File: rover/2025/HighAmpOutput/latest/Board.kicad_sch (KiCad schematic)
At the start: 17 parts, among them J1 JST2_Pin, U1 EC5_Connector, U10 XT60PM-F, U11 XT60PM-F, U12 XT60PM-F, U2 HSS-VN7004SLHTR, U3 XT60-F, U4 XT60-F, U5 XT60-F, U6 XT60-F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

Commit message: .
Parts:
- removed U10, U9: XT60PM-F, RoverFootprint:AMASS_XT60PW-F_1x02_P7.20mm_Horizontal, symbol RoverLibrary:XT60PW-F
- added D2: R, LED_SMD:LED_0805_2012Metric_Pad1.15x1.40mm_HandSolder, symbol RoverLibrary:LED
- added R2: 15k, Resistor_SMD:R_0805_2012Metric_Pad1.20x1.40mm_HandSolder, symbol RoverLibrary:R_0805
- added R5: 1K, Resistor_SMD:R_0805_2012Metric_Pad1.20x1.40mm_HandSolder, symbol RoverLibrary:R_0805
- added U13, U14: XT60-F, RoverFootprint:AMASS_XT60-F_1x02_P7.20mm_Vertical, symbol RoverLibrary:XT60-F
- D1: value LED -> R
- U11, U12: STATUS (none) -> APPROVED
- U2: STATUS TO BE VERIFIED -> APPROVED
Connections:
- net GND: now also R1.2, D2.1 (K), R2.2, U13.1 (-), U14.1 (-); no longer R1.1
- net at J1.1, U2.4 (INPUT): now also R2.1
- net at U2.6 (FR_DIAG): now also R1.1; no longer R1.2
- net +24v renamed +24V
- net +24V: now also R5.1
- net Vinput renamed +24V_I
- net +24V_I: now also U13.2 (+), U14.2 (+)
- new net: D2.2 (A), R5.2
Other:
- moved on the sheet: J1, R1, R4

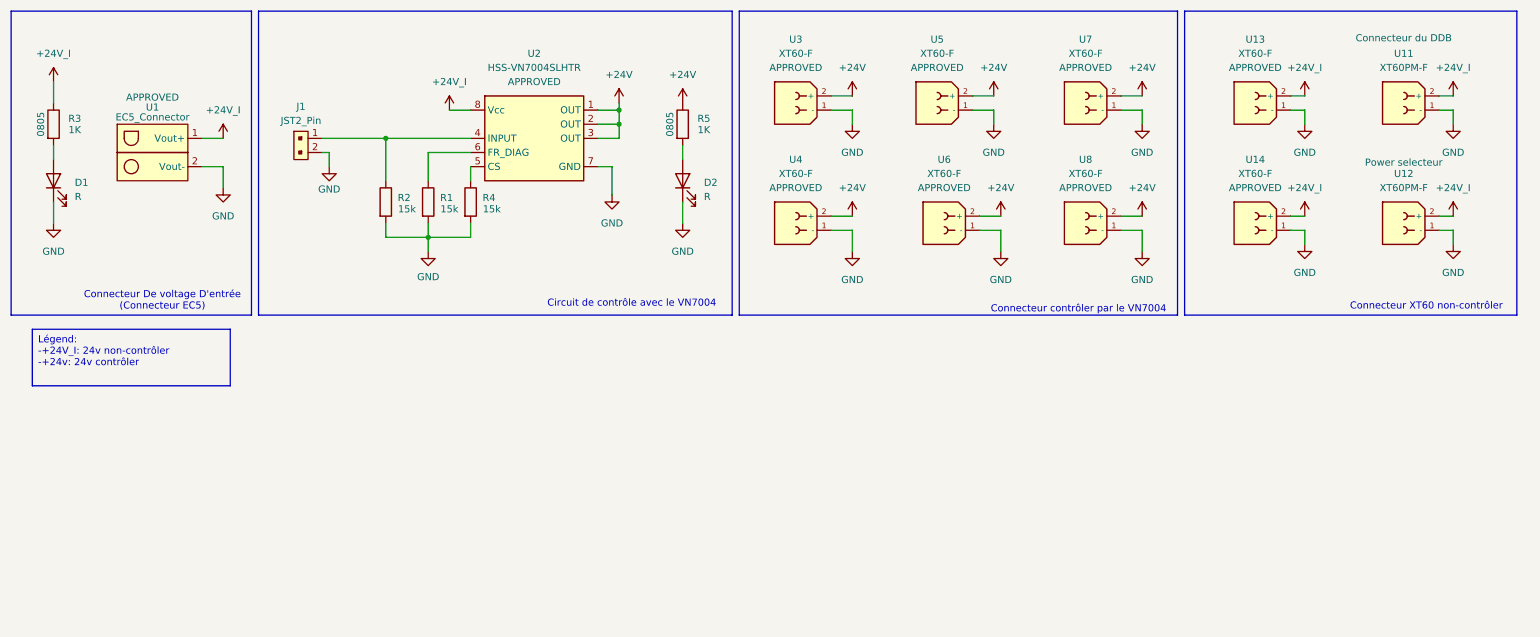
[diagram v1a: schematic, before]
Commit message: Avancement PCB HighAmpOutput
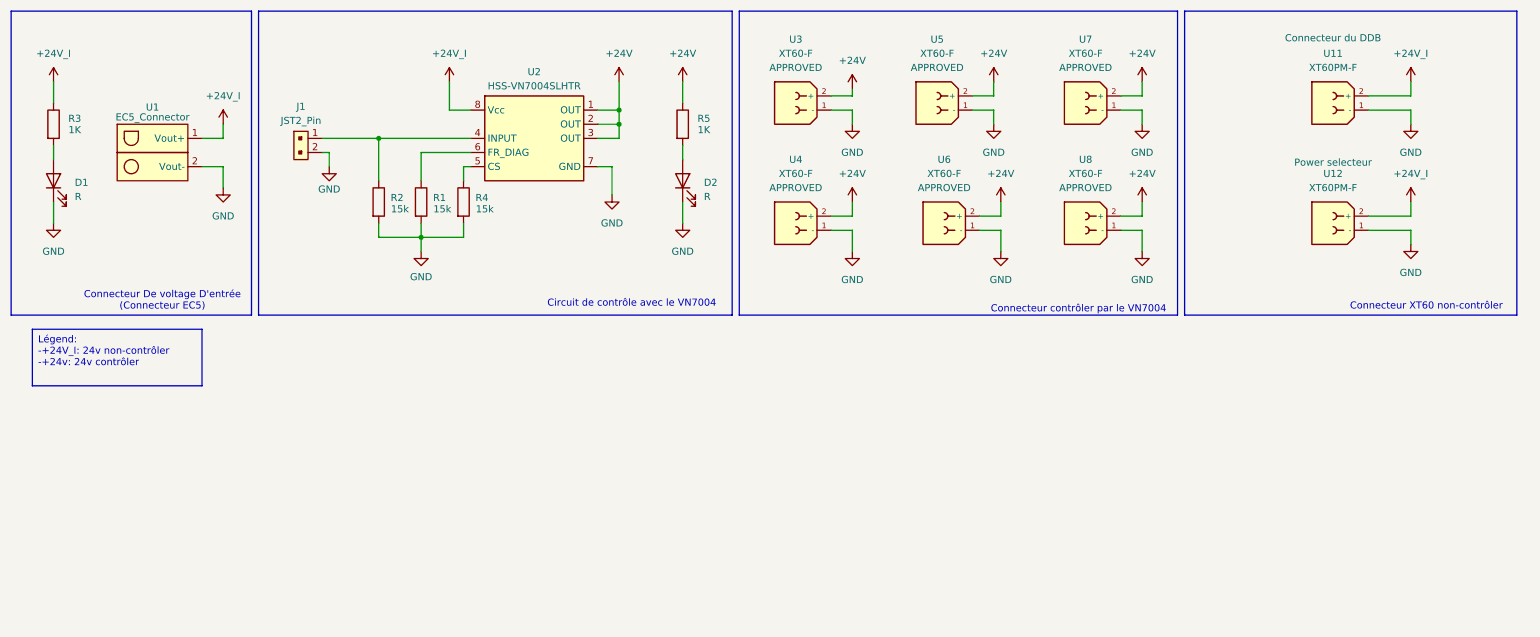
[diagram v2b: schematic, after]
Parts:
- removed U13, U14: XT60-F, RoverFootprint:AMASS_XT60-F_1x02_P7.20mm_Vertical, symbol RoverLibrary:XT60-F
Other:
- moved on the sheet: R1, R2, R4, U11, U12

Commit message: Done
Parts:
- removed J1: JST2_Pin, RoverFootprint:2-pins-JST_XH_B2B-XH-A_1x02_P2.50mm_Vertical, symbol RoverLibrary:CONN-JST-XH-B2B
- added J2: JST-PH-S2B, Connector_JST:JST_PH_B2B-PH-K_1x02_P2.00mm_Vertical, symbol Connector_Generic:Conn_01x02
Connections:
- net GND: now also J2.2 (Pin_2)
- net at R2.1, U2.4 (INPUT): now also J2.1 (Pin_1)
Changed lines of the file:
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@@
 	(wire
 		(pts
-			(xy 69.85 35.56) (xy 80.01 35.56)
+			(xy 72.39 35.56) (xy 80.01 35.56)
 		)
 		(stroke
@@
 	(wire
 		(pts
-			(xy 71.12 38.1) (xy 69.85 38.1)
+			(xy 73.66 38.1) (xy 72.39 38.1)
 		)
 		(stroke
@@
 	(wire
 		(pts
-			(xy 71.12 40.64) (xy 71.12 38.1)
+			(xy 73.66 40.64) (xy 73.66 38.1)
 		)
 		(stroke
@@
 	(symbol
 		(lib_id "power:GND")
-		(at 71.12 40.64 0)
+		(at 73.66 40.64 0)
 		(unit 1)
 		(exclude_from_sim no)
@@
 		(dnp no)
 		(property "Reference" "#PWR06"
-			(at 71.12 46.99 0)
+			(at 73.66 46.99 0)
 			(effects
 				(font
@@
 		)
 		(property "Value" "GND"
-			(at 71.12 44.704 0)
+			(at 73.66 44.704 0)
 			(effects
 				(font
@@
 		)
 		(property "Footprint" ""
-			(at 71.12 40.64 0)
+			(at 73.66 40.64 0)
 			(effects
 				(font
@@
 		)
 		(property "Datasheet" ""
-			(at 71.12 40.64 0)
+			(at 73.66 40.64 0)
 			(effects
 				(font
@@
 		)
 		(property "Description" "Power symbol creates a global label with name \"GND\" , ground"
-			(at 71.12 40.64 0)
+			(at 73.66 40.64 0)
 			(effects
 				(font
@@
 	)
 	(symbol
-		(lib_id "RoverLibrary:CONN-JST-XH-B2B")
-		(at 66.675 32.385 0)
-		(unit 1)
-		(exclude_from_sim no)
-		(in_bom yes)
-		(on_board yes)
-		(dnp no)
-		(fields_autoplaced yes)
-		(property "Reference" "J1"
-			(at 66.04 29.845 0)
-			(effects
-				(font
-					(size 1.27 1.27)
-				)
-			)
-		)
-		(property "Value" "JST2_Pin"
-			(at 66.04 32.385 0)
-			(effects
-				(font
-					(size 1.27 1.27)
-				)
-			)
-		)
-		(property "Footprint" "RoverFootprint:2-pins-JST_XH_B2B-XH-A_1x02_P2.50mm_Vertical"
-			(at 66.675 32.385 0)
-			(effects
-				(font
-					(size 1.27 1.27)
-				)
-				(hide yes)
-			)
-		)
-		(property "Datasheet" ""
-			(at 66.675 32.385 0)
-			(effects
-				(font
-					(size 1.27 1.27)
-				)
-				(hide yes)
-			)
-		)
-		(property "Description" ""
-			(at 66.675 32.385 0)
-			(effects
-				(font
-					(size 1.27 1.27)
-				)
-				(hide yes)
-			)
-		)
-		(pin "1"
-		)
-		(pin "2"
-		)
-		(instances
-			(project "Template"
-				(path "/a4fa9b30-7b48-474a-bdaa-0d7a6d26a697/8da6c8a9-d96a-428b-ac41-906630b726a3"
-					(reference "J1")
-					(unit 1)
-				)
-			)
-		)
-	)
-	(symbol
 		(lib_id "power:GND")
 		(at 134.62 50.8 0)
@@
 					(unit 1)
 				)
+			)
+		)
+	)
+	(symbol
+		(lib_id "Connector_Generic:Conn_01x02")
+		(at 67.31 35.56 0)
+		(mirror y)
+		(unit 1)
+		(exclude_from_sim no)
+		(in_bom yes)
+		(on_board yes)
+		(dnp no)
+		(fields_autoplaced yes)
+		(property "Reference" "J2"
+			(at 67.31 29.21 0)
+			(effects
+				(font
+					(size 1.27 1.27)
+				)
+			)
+		)
+		(property "Value" "JST-PH-S2B"
+			(at 67.31 31.75 0)
+			(effects
+				(font
+					(size 1.27 1.27)
+				)
+			)
+		)
+		(property "Footprint" "Connector_JST:JST_PH_B2B-PH-K_1x02_P2.00mm_Vertical"
+			(at 67.31 35.56 0)
+			(effects
+				(font
+					(size 1.27 1.27)
+				)
+				(hide yes)
+			)
+		)
+		(property "Datasheet" "~"
+			(at 67.31 35.56 0)
+			(effects
+				(font
+					(size 1.27 1.27)
+				)
+				(hide yes)
+			)
+		)
+		(property "Description" "Generic connector, single row, 01x02, script generated (kicad-library-utils/schlib/autogen/connector/)"
+			(at 67.31 35.56 0)
+			(effects
+				(font
+					(size 1.27 1.27)
+				)
+				(hide yes)
+			)
+		)
+		(pin "2"
+		)
+		(pin "1"
+		)
+		(instances
+			(project ""
+				(path "/a4fa9b30-7b48-474a-bdaa-0d7a6d26a697/8da6c8a9-d96a-428b-ac41-906630b726a3"
+					(reference "J2")
+					(unit 1)
+				)

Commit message: HighAmp generated
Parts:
- J2: value JST-PH-S2B -> JST-PH-B2B
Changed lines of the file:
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@@
 			)
 		)
-		(property "Value" "JST-PH-S2B"
+		(property "Value" "JST-PH-B2B"
 			(at 67.31 31.75 0)
 			(effects

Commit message: HighAMP_Rch_ADD_to_INPUT_to_7004
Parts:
- added R6: 15k, Resistor_SMD:R_0805_2012Metric_Pad1.20x1.40mm_HandSolder, symbol RoverLibrary:R_0805
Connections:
- net at J2.1 (Pin_1), R2.1: now also R6.1; no longer U2.4 (INPUT)
- new net: R6.2, U2.4 (INPUT)
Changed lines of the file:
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@@
+	)
+	(junction
+		(at 123.19 30.48)
+		(diameter 0)
+		(color 0 0 0 0)
 	)
 	(junction
@@
 	)
 	(junction
-		(at 123.19 30.48)
-		(diameter 0)
-		(color 0 0 0 0)
-	)
-	(junction
 		(at 123.19 33.02)
 		(diameter 0)
@@
 	(wire
 		(pts
+			(xy 91.44 35.56) (xy 96.52 35.56)
+		)
+		(stroke
+			(width 0)
+			(type default)
+		)
+	)
+	(wire
+		(pts
 			(xy 217.17 52.07) (xy 217.17 55.88)
 		)
@@
 	(wire
 		(pts
+			(xy 80.01 35.56) (xy 83.82 35.56)
+		)
+		(stroke
+			(width 0)
+			(type default)
+		)
+	)
+	(wire
+		(pts
 			(xy 265.43 33.02) (xy 265.43 30.48)
 		)
@@
 		(pts
 			(xy 21.59 25.4) (xy 21.59 29.21)
-		)
-		(stroke
-			(width 0)
-			(type default)
-		)
-	)
-	(wire
-		(pts
-			(xy 80.01 35.56) (xy 96.52 35.56)
 		)
 		(stroke
@@
 					(unit 1)
 				)
+			)
+		)
+	)
+	(symbol
+		(lib_id "RoverLibrary:R_0805")
+		(at 87.63 35.56 90)
+		(unit 1)
+		(exclude_from_sim no)
+		(in_bom yes)
+		(on_board yes)
+		(dnp no)
+		(property "Reference" "R6"
+			(at 88.138 32.512 90)
+			(do_not_autoplace yes)
+			(effects
+				(font
+					(size 1.27 1.27)
+				)
+			)
+		)
+		(property "Value" "15k"
+			(at 87.63 30.48 90)
+			(do_not_autoplace yes)
+			(effects
+				(font
+					(size 1.27 1.27)
+				)
+			)
+		)
+		(property "Footprint" "Resistor_SMD:R_0805_2012Metric_Pad1.20x1.40mm_HandSolder"
+			(at 87.63 43.18 90)
+			(effects
+				(font
+					(size 1.27 1.27)
+				)
+				(hide yes)
+			)
+		)
+		(property "Datasheet" ""
+			(at 87.63 35.56 90)
+			(do_not_autoplace yes)
+			(effects
+				(font
+					(size 1.27 1.27)
+				)
+				(hide yes)
+			)
+		)
+		(property "Description" "Resistor"
+			(at 99.06 35.56 0)
+			(effects
+				(font
+					(size 1.27 1.27)
+				)
+				(hide yes)
+			)
+		)
+		(property "Digikey" ""
+			(at 87.63 35.56 0)
+			(do_not_autoplace yes)
+			(effects
+				(font
+					(size 1.27 1.27)
+				)
+				(hide yes)
+			)
+		)
+		(property "Package" "0805"
+			(at 87.63 37.846 90)
+			(do_not_autoplace yes)
+			(effects
+				(font
+					(size 1.27 1.27)
+				)
+				(hide yes)
+			)
+		)
+		(pin "2"
+		)
+		(pin "1"
+		)
+		(instances
+			(project "HighAmpOutput"
+				(path "/a4fa9b30-7b48-474a-bdaa-0d7a6d26a697/8da6c8a9-d96a-428b-ac41-906630b726a3"
+					(reference "R6")
+					(unit 1)
+				)

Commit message: Update
update pour préparer pour la V2
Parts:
- removed R2: 15k, Resistor_SMD:R_0805_2012Metric_Pad1.20x1.40mm_HandSolder, symbol RoverLibrary:R_0805
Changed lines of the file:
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@@
-	)
-	(junction
-		(at 80.01 35.56)
-		(diameter 0)
-		(color 0 0 0 0)
 	)
 	(junction
@@
 	(wire
 		(pts
-			(xy 72.39 35.56) (xy 80.01 35.56)
-		)
-		(stroke
-			(width 0)
-			(type default)
-		)
-	)
-	(wire
-		(pts
 			(xy 92.71 30.48) (xy 96.52 30.48)
 		)
@@
 	(wire
 		(pts
-			(xy 80.01 35.56) (xy 80.01 43.18)
-		)
-		(stroke
-			(width 0)
-			(type default)
-		)
-	)
-	(wire
-		(pts
 			(xy 52.07 35.56) (xy 52.07 33.02)
 		)
@@
 	(wire
 		(pts
-			(xy 80.01 35.56) (xy 83.82 35.56)
+			(xy 72.39 35.56) (xy 83.82 35.56)
 		)
 		(stroke
@@
 	(wire
 		(pts
-			(xy 80.01 50.8) (xy 80.01 53.34)
-		)
-		(stroke
-			(width 0)
-			(type default)
-		)
-	)
-	(wire
-		(pts
 			(xy 217.17 49.53) (xy 217.17 46.99)
 		)
@@
 		(pts
 			(xy 187.96 49.53) (xy 191.77 49.53)
-		)
-		(stroke
-			(width 0)
-			(type default)
-		)
-	)
-	(wire
-		(pts
-			(xy 80.01 53.34) (xy 87.63 53.34)
 		)
 		(stroke
@@
 				(size 1.27 1.27)
 				(thickness 0.1588)
-				(color 132 0 0 1)
+				(color 0 0 0 1)
+			)
+			(justify left top)
+		)
+	)
+	(text_box "-Ajouter un ventilateur?\n-Dissipation de chaleur répartis sur les différentes layeur"
+		(exclude_from_sim no)
+		(at 139.7 109.22 0)
+		(size 34.29 13.97)
+		(stroke
+			(width 0)
+			(type default)
+			(color 132 0 0 1)
+		)
+		(fill
+			(type color)
+			(color 255 255 194 1)
+		)
+		(effects
+			(font
+				(size 1.27 1.27)
+				(color 0 0 0 1)
 			)
 			(justify left top)
@@
 					(unit 1)
 				)
-			)
-		)
-	)
-	(symbol
-		(lib_id "RoverLibrary:R_0805")
-		(at 80.01 46.99 0)
-		(unit 1)
-		(exclude_from_sim no)
-		(in_bom yes)
-		(on_board yes)
-		(dnp no)
-		(property "Reference" "R2"
-			(at 83.312 46.228 0)
-			(do_not_autoplace yes)
-			(effects
-				(font
-					(size 1.27 1.27)
-				)
-			)
-		)
-		(property "Value" "15k"
-			(at 83.82 48.26 0)
-			(do_not_autoplace yes)
-			(effects
-				(font
-					(size 1.27 1.27)
-				)
-			)
-		)
-		(property "Footprint" "Resistor_SMD:R_0805_2012Metric_Pad1.20x1.40mm_HandSolder"
-			(at 72.39 46.99 90)
-			(effects
-				(font
-					(size 1.27 1.27)
-				)
-				(hide yes)
-			)
-		)
-		(property "Datasheet" ""
-			(at 80.01 46.99 90)
-			(do_not_autoplace yes)
-			(effects
-				(font
-					(size 1.27 1.27)
-				)
-				(hide yes)
-			)
-		)
-		(property "Description" "Resistor"
-			(at 80.01 58.42 0)
-			(effects
-				(font
-					(size 1.27 1.27)
-				)
-				(hide yes)
-			)
-		)
-		(property "Digikey" ""
-			(at 80.01 46.99 0)
-			(do_not_autoplace yes)
-			(effects
-				(font
-					(size 1.27 1.27)
-				)
-				(hide yes)
-			)
-		)
-		(property "Package" "0805"
-			(at 77.724 46.99 90)
-			(do_not_autoplace yes)
-			(effects
-				(font
-					(size 1.27 1.27)
-				)
-				(hide yes)
-			)
-		)
-		(pin "2"
-		)
-		(pin "1"
-		)
-		(instances
-			(project "HighAmpOutput"
-				(path "/a4fa9b30-7b48-474a-bdaa-0d7a6d26a697/8da6c8a9-d96a-428b-ac41-906630b726a3"
-					(reference "R2")
-					(unit 1)
-				)

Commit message: update_v2_highampoutput
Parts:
- added C1: 1n, Capacitor_SMD:C_0805_2012Metric_Pad1.18x1.45mm_HandSolder, symbol RoverLibrary:C_0805
- added J1: Conn_01x03, Connector_JST:JST_PH_B3B-PH-K_1x03_P2.00mm_Vertical, symbol RoverLibrary:Conn_01x03
- added R2: 100k, Resistor_SMD:R_0805_2012Metric_Pad1.20x1.40mm_HandSolder, symbol RoverLibrary:R_0805
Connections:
- net +24V: now also J1.1 (Pin_1)
- net GND: now also C1.2, J1.3 (Pin_3), R2.2; no longer J2.2 (Pin_2)
- net at R6.2, U2.4 (INPUT): now also R2.1
- new net: C1.1, J2.2 (Pin_2)
- no-connect marks 0 -> 1
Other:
- moved on the sheet: J2, R6, U11, U12

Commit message: V2_UPdate_HighAMP
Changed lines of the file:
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@@
-		)
-	)
-	(text_box "-Ajouter un ventilateur?\n-Dissipation de chaleur répartis sur les différentes layeur"
-		(exclude_from_sim no)
-		(at 69.85 71.12 0)
-		(size 34.29 13.97)
-		(stroke
-			(width 0)
-			(type default)
-			(color 132 0 0 1)
-		)
-		(fill
-			(type color)
-			(color 255 255 194 1)
-		)
-		(effects
-			(font
-				(size 1.27 1.27)
-				(color 0 0 0 1)
-			)
-			(justify left top)
 		)
 	)
